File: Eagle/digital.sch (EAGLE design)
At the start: 49 parts, among them IC1 L4931CZ33-AP

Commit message: Added level shifting
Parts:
- added IC2: 74HCT08D, 74xx-eu:74HCT08D
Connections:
- new net N$46: IC2A.I0, IC2A.I1, U$4.MISO
- net +5V/2: now also IC2P.VCC
- net DGND: now also IC2P.GND
- net N$6: now also IC2A.O; no longer U$4.MISO
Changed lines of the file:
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@@
 <part name="S1" library="switch" deviceset="9070-1W" device=""/>
 <part name="SUPPLY58" library="supply2" deviceset="DGND" device=""/>
+<part name="IC2" library="74xx-eu" deviceset="74*08" device="D" technology="HCT"/>
+<part name="SUPPLY9" library="supply2" deviceset="DGND" device=""/>
+<part name="SUPPLY59" library="supply2" deviceset="+5V/2" device=""/>
 </parts>
 <sheets>
@@
 <instance part="S1" gate="2" x="358.14" y="-10.16" rot="MR90"/>
 <instance part="SUPPLY58" gate="G$1" x="370.84" y="-7.62"/>
+<instance part="IC2" gate="A" x="121.92" y="27.94" rot="R180"/>
+<instance part="IC2" gate="P" x="213.36" y="53.34"/>
+<instance part="SUPPLY9" gate="G$1" x="213.36" y="43.18"/>
+<instance part="SUPPLY59" gate="G$1" x="213.36" y="63.5"/>
 </instances>
 <busses>
@@
 <junction x="363.22" y="-2.54"/>
 </segment>
+<segment>
+<pinref part="IC2" gate="P" pin="GND"/>
+<pinref part="SUPPLY9" gate="G$1" pin="DGND"/>
+</segment>
 </net>
 <net name="N$26" class="0">
@@
 <pinref part="SUPPLY4" gate="G$1" pin="+5V/2"/>
 </segment>
+<segment>
+<pinref part="IC2" gate="P" pin="VCC"/>
+<pinref part="SUPPLY59" gate="G$1" pin="+5V/2"/>
+</segment>
 </net>
 <net name="N$10" class="0">
@@
 <wire x1="15.24" y1="33.02" x2="45.72" y2="33.02" width="0.1524" layer="91"/>
 <wire x1="45.72" y1="33.02" x2="45.72" y2="30.48" width="0.1524" layer="91"/>
-<wire x1="45.72" y1="30.48" x2="144.78" y2="30.48" width="0.1524" layer="91"/>
-<wire x1="144.78" y1="30.48" x2="144.78" y2="33.02" width="0.1524" layer="91"/>
-<pinref part="U$4" gate="G$1" pin="MISO"/>
-<wire x1="144.78" y1="33.02" x2="149.86" y2="33.02" width="0.1524" layer="91"/>
+<pinref part="IC2" gate="A" pin="O"/>
+<wire x1="45.72" y1="30.48" x2="114.3" y2="30.48" width="0.1524" layer="91"/>
+<wire x1="114.3" y1="30.48" x2="114.3" y2="27.94" width="0.1524" layer="91"/>
 </segment>
 </net>
@@
 <wire x1="15.24" y1="27.94" x2="45.72" y2="27.94" width="0.1524" layer="91"/>
 <wire x1="45.72" y1="27.94" x2="45.72" y2="25.4" width="0.1524" layer="91"/>
-<wire x1="45.72" y1="25.4" x2="147.32" y2="25.4" width="0.1524" layer="91"/>
-<wire x1="147.32" y1="25.4" x2="147.32" y2="30.48" width="0.1524" layer="91"/>
+<wire x1="45.72" y1="25.4" x2="96.52" y2="25.4" width="0.1524" layer="91"/>
+<wire x1="96.52" y1="25.4" x2="96.52" y2="20.32" width="0.1524" layer="91"/>
+<wire x1="96.52" y1="20.32" x2="147.32" y2="20.32" width="0.1524" layer="91"/>
+<wire x1="147.32" y1="20.32" x2="147.32" y2="30.48" width="0.1524" layer="91"/>
 <pinref part="U$4" gate="G$1" pin="SCK"/>
 <wire x1="147.32" y1="30.48" x2="149.86" y2="30.48" width="0.1524" layer="91"/>
@@
 </segment>
 </net>
+<net name="N$46" class="0">
+<segment>
+<pinref part="U$4" gate="G$1" pin="MISO"/>
+<wire x1="144.78" y1="33.02" x2="149.86" y2="33.02" width="0.1524" layer="91"/>
+<wire x1="144.78" y1="30.48" x2="144.78" y2="33.02" width="0.1524" layer="91"/>
+<pinref part="IC2" gate="A" pin="I1"/>
+<pinref part="IC2" gate="A" pin="I0"/>
+<wire x1="129.54" y1="30.48" x2="129.54" y2="25.4" width="0.1524" layer="91"/>
+<wire x1="144.78" y1="30.48" x2="129.54" y2="30.48" width="0.1524" layer="91"/>
+<junction x="129.54" y="30.48"/>
+</segment>
+</net>

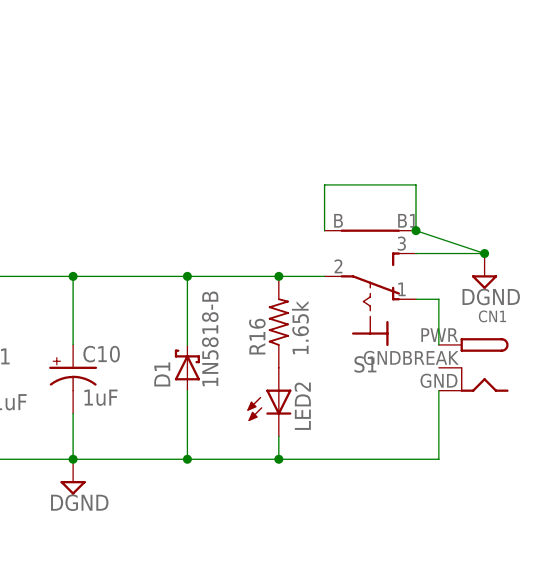
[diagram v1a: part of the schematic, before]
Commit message: Board shrink
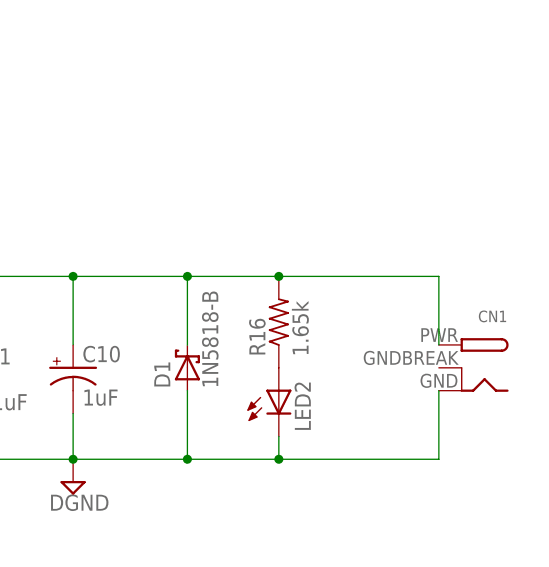
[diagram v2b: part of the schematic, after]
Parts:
- removed S1: (no value), switch:9070-1W
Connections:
- removed net N$44: CN1.PWR, S1.O
- net +5V/2: now also CN1.PWR; no longer S1.P
- net DGND: no longer S1.B, S1.B1, S1.S
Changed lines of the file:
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@@
 <part name="SUPPLY7" library="supply2" deviceset="DGND" device=""/>
 <part name="U$5" library="SparkFun-Connectors" deviceset="USB" device="SMD"/>
-<part name="S1" library="switch" deviceset="9070-1W" device=""/>
-<part name="SUPPLY58" library="supply2" deviceset="DGND" device=""/>
 <part name="IC2" library="74xx-eu" deviceset="74*08" device="D" technology="HCT"/>
 <part name="SUPPLY9" library="supply2" deviceset="DGND" device=""/>
@@
 <instance part="SUPPLY7" gate="G$1" x="167.64" y="7.62"/>
 <instance part="U$5" gate="G$1" x="71.12" y="12.7"/>
-<instance part="S1" gate="2" x="358.14" y="-10.16" rot="MR90"/>
-<instance part="SUPPLY58" gate="G$1" x="370.84" y="-7.62"/>
 <instance part="IC2" gate="A" x="121.92" y="27.94" rot="R180"/>
 <instance part="IC2" gate="P" x="213.36" y="53.34"/>
@@
 </segment>
 <segment>
-<pinref part="S1" gate="2" pin="S"/>
-<pinref part="S1" gate="2" pin="B1"/>
-<wire x1="370.84" y1="-5.08" x2="363.22" y2="-2.54" width="0.1524" layer="91"/>
-<pinref part="SUPPLY58" gate="G$1" pin="DGND"/>
-<junction x="370.84" y="-5.08"/>
-<wire x1="370.84" y1="-5.08" x2="363.22" y2="-5.08" width="0.1524" layer="91"/>
-<pinref part="S1" gate="2" pin="B"/>
-<wire x1="353.06" y1="-2.54" x2="353.06" y2="2.54" width="0.1524" layer="91"/>
-<wire x1="353.06" y1="2.54" x2="363.22" y2="2.54" width="0.1524" layer="91"/>
-<wire x1="363.22" y1="2.54" x2="363.22" y2="-2.54" width="0.1524" layer="91"/>
-<junction x="363.22" y="-2.54"/>
-</segment>
-<segment>
 <pinref part="IC2" gate="P" pin="GND"/>
 <pinref part="SUPPLY9" gate="G$1" pin="DGND"/>
@@
 <junction x="304.8" y="-7.62"/>
 <pinref part="R16" gate="G$1" pin="2"/>
-<pinref part="S1" gate="2" pin="P"/>
-<wire x1="347.98" y1="-7.62" x2="353.06" y2="-7.62" width="0.1524" layer="91"/>
 <junction x="347.98" y="-7.62"/>
+<pinref part="CN1" gate="G$1" pin="PWR"/>
+<wire x1="365.76" y1="-7.62" x2="365.76" y2="-15.24" width="0.1524" layer="91"/>
+<wire x1="365.76" y1="-7.62" x2="347.98" y2="-7.62" width="0.1524" layer="91"/>
 </segment>
 <segment>
@@
 </segment>
 </net>
-<net name="N$44" class="0">
-<segment>
-<pinref part="S1" gate="2" pin="O"/>
-<pinref part="CN1" gate="G$1" pin="PWR"/>
-<wire x1="363.22" y1="-10.16" x2="365.76" y2="-10.16" width="0.1524" layer="91"/>
-<wire x1="365.76" y1="-10.16" x2="365.76" y2="-15.24" width="0.1524" layer="91"/>
-</segment>
-</net>
